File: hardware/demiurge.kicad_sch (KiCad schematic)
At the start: 58 parts, among them J2 PGM, U5 AMS1117-3.3, U6 74LVC1T45W6, U7 CH32V307RCT6, Y1 25MHz

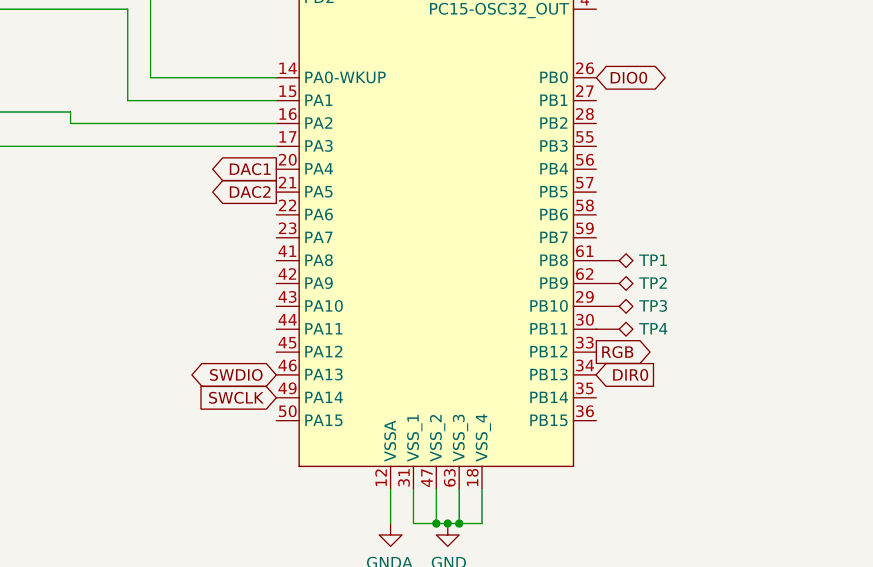
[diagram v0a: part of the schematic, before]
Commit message: Added USB1/USB2 labels. What should we do with 2 USB ports?
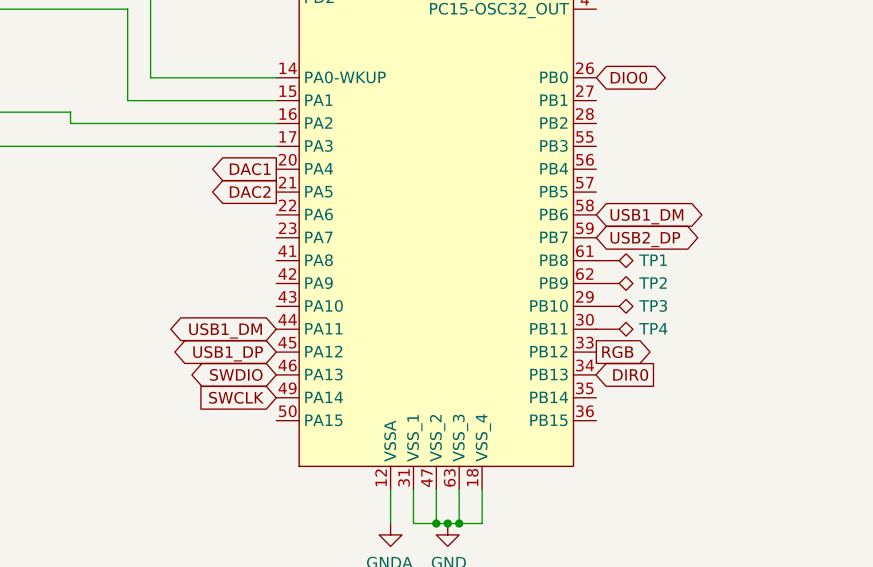
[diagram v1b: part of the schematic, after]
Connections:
- net USB1_DM: now reaches U7.44 (PA11)
- net USB1_DM: now also U7.58 (PB6)
- net USB1_DP: now reaches U7.45 (PA12)
- net USB2_DP: now reaches U7.59 (PB7)
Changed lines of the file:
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@@
+    )
+  )
+  (global_label "USB2_DP" (shape bidirectional) (at 266.7 142.24 0) (fields_autoplaced)
+    (effects (font (size 1.27 1.27)) (justify left))
+    (property "Intersheet References" "${INTERSHEET_REFS}" (id 0) (at 277.5513 142.3194 0)
+      (effects (font (size 1.27 1.27)) (justify left) hide)
     )
   )
@@
     (property "Intersheet References" "${INTERSHEET_REFS}" (id 0) (at 273.6809 93.9006 0)
       (effects (font (size 1.27 1.27)) (justify left) hide)
+    )
+  )
+  (global_label "USB1_DM" (shape bidirectional) (at 231.14 152.4 180) (fields_autoplaced)
+    (effects (font (size 1.27 1.27)) (justify right))
+    (property "Intersheet References" "${INTERSHEET_REFS}" (id 0) (at 220.1072 152.3206 0)
+      (effects (font (size 1.27 1.27)) (justify right) hide)
     )
   )
@@
     (effects (font (size 1.27 1.27)) (justify right))
     (property "Intersheet References" "${INTERSHEET_REFS}" (id 0) (at 342.2691 118.0306 0)
+      (effects (font (size 1.27 1.27)) (justify right) hide)
+    )
+  )
+  (global_label "USB1_DP" (shape bidirectional) (at 231.14 154.94 180) (fields_autoplaced)
+    (effects (font (size 1.27 1.27)) (justify right))
+    (property "Intersheet References" "${INTERSHEET_REFS}" (id 0) (at 220.2887 154.8606 0)
       (effects (font (size 1.27 1.27)) (justify right) hide)
     )
@@
       (effects (font (size 1.27 1.27)) (justify left) hide)
     )
+  )
+  (global_label "USB1_DM" (shape bidirectional) (at 266.7 139.7 0) (fields_autoplaced)
+    (effects (font (size 1.27 1.27)) (justify left))
+    (property "Intersheet References" "${INTERSHEET_REFS}" (id 0) (at 277.7328 139.7794 0)
+      (effects (font (size 1.27 1.27)) (justify left) hide)
+    )

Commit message: First cut of the software. Not changed to RISC-V yet.
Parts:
- removed C16, C19, C2, C8: 100nF, Capacitor_SMD:C_0603_1608Metric, symbol Device:C
- removed R1, R10, R2, R3, R4, R7, R8, R9: 10k, Resistor_SMD:R_0603_1608Metric, symbol Device:R
- removed SW1, SW2, SW3, SW4: ~, Button_Switch_THT:SW_PUSH_6mm_H8mm, symbol Switch:SW_Push
- added D13: ~, Diode_SMD:D_SOD-123, symbol Device:D_Schottky
- added J10: (no value), symbol Connector:USB_C_Receptacle_USB2.0
- added J11: (no value), symbol Connector:USB_A
- added R51: 10k, Resistor_SMD:R_0603_1608Metric, symbol Device:R
- added R52, R53: 5.1k, Resistor_SMD:R_0402_1005Metric, symbol Device:R
- added R54, R55: 22R, Resistor_SMD:R_0402_1005Metric, symbol Device:R
- C31: value 12pF -> 20pF; LCSC C1547 -> C1648
- U6: value 74LVC1T45W6 -> (none); LCSC C168856 -> C441819
- Y1: value 25MHz -> 16MHz; LCSC C90913 -> C13738
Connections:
- net +5V: now also D13.1 (K), J11.1 (VBUS)
- net 0: now also R51.1
- net DIR0: now also U7.27 (PB1)
- net GND: now also J10.A1 (GND), J10.A12 (GND), J10.B1 (GND), J10.B12 (GND), J10.S1 (SHIELD), J11.4 (GND), J11.5 (Shield), R51.2, R52.2, R53.2
- net USB1_DM: now also R54.2; no longer U7.58 (PB6)
- net USB1_DP: now also R55.2
- net USB2_DP: now also J11.3 (D+)
- net at TP3.1: now also U7.53 (PC12); no longer U7.29 (PB10)
- net SWO: now reaches J2.6 (Pin_6)
- net SWO: now also U7.55 (PB3)
- net at TP4.1: now also U7.54 (PD2); no longer U7.30 (PB11)
- net at TP1.1: now also U7.51 (PC10); no longer U7.61 (PB8)
- net at TP2.1: now also U7.52 (PC11); no longer U7.62 (PB9)
- net Pot+LED/GPRST: now reaches U7.34 (PB13)
- net Pot+LED/GPINT: now reaches U7.35 (PB14)
- net LED1: no longer names the net of U7.37 (PC6)
- net LED2: no longer names the net of U7.38 (PC7)
- net LED3: no longer names the net of U7.39 (PC8)
- net LED4: no longer names the net of U7.40 (PC9)
- net RGB: no longer names the net of U7.33 (PB12)
- new net: J10.A5 (CC1), R52.1
- new net: J10.A6 (D+), J10.B6 (D+), R55.1
- new net: J10.A7 (D-), J10.B7 (D-), R54.1
- new net: J10.B5 (CC2), R53.1
- new net Pot+LED/SCL: U7.29 (PB10)
- new net Pot+LED/SDA: U7.30 (PB11)
- new net USB2_DM: J11.2 (D-), U7.58 (PB6)
- new net VBUS: D13.2 (A), J10.A4 (VBUS), J10.A9 (VBUS), J10.B4 (VBUS), J10.B9 (VBUS)
- no-connect marks 8 -> 11
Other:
- sheet Pot+LED ports: added GPINT, GPRST, SCL, SDA; removed LED1, LED2, LED3, LED4, RGB
- note added: "22uF + 100nF at each VDD/VSS pin on CPU"
- note added: "Input Filter"
- note added: "Power"
- note added: "Programming"
- note added: "Unclear if GND and GNDA should be connected externally, or kept separated to avoid ground loop. Keeping this open for now, until we know better."
- note removed: "At input"
- moved on the sheet: C1, C10, C11, C12, C13, C14, C15, C17, C18, C20, C21, C3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

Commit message: Rev E updated to Rev F (WIP)
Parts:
- removed D13: ~, Diode_SMD:D_SOD-123, symbol Device:D_Schottky
- removed J10: (no value), symbol Connector:USB_C_Receptacle_USB2.0
- removed J11: (no value), symbol Connector:USB_A
- removed J2: PGM, Connector_PinHeader_2.54mm:PinHeader_2x03_P2.54mm_Vertical, symbol Connector_Generic:Conn_02x03_Odd_Even
- removed JP2: SolderJumper_2_Open, Jumper:SolderJumper-2_P1.3mm_Open_TrianglePad1.0x1.5mm, symbol Jumper:SolderJumper_2_Open
- removed R51: 10k, Resistor_SMD:R_0603_1608Metric, symbol Device:R
- removed R52: 5.1k, Resistor_SMD:R_0402_1005Metric, symbol Device:R
- removed R55: 22R, Resistor_SMD:R_0402_1005Metric, symbol Device:R
- removed TP1, TP2, TP3, TP4: ~, aaa:TestPoint_THTPad_1.0x1.0mm_Drill0.6mm, symbol Connector:TestPoint_Alt
- removed U7: CH32V307RCT6, Package_QFP:LQFP-64_10x10mm_P0.5mm, symbol awesomeaudio:CH32V307RCT6
- removed Y1: 16MHz, Crystal:Crystal_SMD_3225-4Pin_3.2x2.5mm, symbol Device:Crystal_GND24_Small
- added C17, C18, C2, C20, C22, C23, C24, C27, C35, C36, C8, C9: 100nF, Capacitor_SMD:C_0603_1608Metric, symbol Device:C
- added C28, C29: 20pF, Capacitor_SMD:C_0603_1608Metric, symbol Device:C
- added C38, C39: 1nF, Capacitor_SMD:C_0603_1608Metric, symbol Device:C
- added D1, D5: ~, Diode_SMD:D_SOD-123, symbol Device:D_Schottky
- added D10, D11, D12, D13: ~, LED_THT:LED_D5.0mm-4_RGB, symbol Device:LED_RAGB
- added J11: ~, aaa:USB_C_Receptacle_Vertical, symbol demiurge-rescue:USB_C_Receptacle_USB2.0-Connector
- added J12: Micro_SD_Card_Det_Hirose_DM3AT, Connector_Card:microSD_HC_Hirose_DM3AT-SF-PEJM5, symbol Connector:Micro_SD_Card_Det_Hirose_DM3AT
- added J2: Conn_01x06, Connector_PinHeader_2.54mm:PinHeader_1x06_P2.54mm_Vertical, symbol Connector_Generic:Conn_01x06
- added J3, J4, J5, J6, J8, J9: ~, aaa:PJ301M-12, symbol Connector:AudioJack2_SwitchT
- added JP2, JP3: ~, Jumper:SolderJumper-2_P1.3mm_Open_RoundedPad1.0x1.5mm, symbol Jumper:Jumper_2_Open
- added R1, R10, R13, R2, R29, R3, R37, R38, R4, R47, R48, R7, R8, R9: 10k, Resistor_SMD:R_0603_1608Metric, symbol Device:R
- added R12: 22R, Resistor_SMD:R_0402_1005Metric, symbol Device:R
- added R14, R15: 5.1k, Resistor_SMD:R_0402_1005Metric, symbol Device:R
- added R16, R18: 18k, Resistor_SMD:R_0603_1608Metric, symbol Device:R
- added R17, R19: 13k, Resistor_SMD:R_0603_1608Metric, symbol Device:R
- added R20, R21, R22, R23, R49, R50: 20k, Resistor_SMD:R_0603_1608Metric, symbol Device:R
- added R24, R25, R26, R27: 3k3, Resistor_SMD:R_0603_1608Metric, symbol Device:R
- added R39, R41: 36k, Resistor_SMD:R_0603_1608Metric, symbol Device:R
- added R40, R42: 22k, Resistor_SMD:R_0603_1608Metric, symbol Device:R
- added R44, R46: 33k, Resistor_SMD:R_0603_1608Metric, symbol Device:R
- added RV1, RV2, RV3, RV4: ~, aaa:Potentiometer_Alpha_RD901F-40-00D_Single_Vertical, symbol Device:R_Potentiometer
- added SW1, SW2, SW3, SW4: ~, Button_Switch_THT:SW_PUSH_6mm_H8mm, symbol Switch:SW_Push
- added TP1: TP1, TestPoint:TestPoint_Pad_1.5x1.5mm, symbol Connector:TestPoint
- added TP2: TP2, TestPoint:TestPoint_Pad_1.5x1.5mm, symbol Connector:TestPoint
- added TP3: SWO, TestPoint:TestPoint_Pad_1.5x1.5mm, symbol Connector:TestPoint
- added U1, U3: MCP6002, Package_SO:SOIC-8_3.9x4.9mm_P1.27mm, symbol Amplifier_Operational:TL072
- added U10, U11, U7, U8: TL072, Package_SO:SOIC-8_3.9x4.9mm_P1.27mm, symbol Amplifier_Operational:TL072
- added U13: CH32V307RCT6, Package_QFP:LQFP-64_10x10mm_P0.5mm, symbol awesomeaudio:CH32V307RCT6
- added U4: AW9523BTQR, Package_DFN_QFN:VQFN-24-1EP_4x4mm_P0.5mm_EP2.45x2.45mm, symbol aaa:AW9523BTQR
- added U5: W25Q128JVS, Package_SO:SOIC-8_5.23x5.23mm_P1.27mm, symbol Memory_Flash:W25Q128JVS
- added Y1: 16MHz, Crystal:Crystal_SMD_3225-4Pin_3.2x2.5mm, symbol Device:Crystal
- C1, C3, C4, C5, C6, C7: LCSC C45783 -> C129303
- C10: renamed from C9; LCSC C45783 -> C129303
- C11: renamed from C10; LCSC C45783 -> C129303
- C12: renamed from C11; LCSC C45783 -> C129303
- C13: renamed from C12; LCSC C45783 -> C129303
- C14: renamed from C13; LCSC C45783 -> C129303
- C15: renamed from C14; LCSC C45783 -> C129303
- C16: renamed from C15; LCSC C45783 -> C129303
- C19: renamed from C17; LCSC C45783 -> C129303
- C30: value 12pF -> 100nF; LCSC C1547 -> C14663
- C31: value 20pF -> 100nF; LCSC C1648 -> C14663
- C34: value 22uF -> 100nF; footprint Capacitor_SMD:C_0805_2012Metric -> Capacitor_SMD:C_0603_1608Metric; LCSC C45783 -> C14663
- J1: LCSC (none) -> C68234
- JP1: footprint Jumper:SolderJumper-3_P1.3mm_Bridged12_Pad1.0x1.5mm -> Jumper:SolderJumper-3_P1.3mm_Bridged12_RoundedPad1.0x1.5mm
- R11: value 10k -> 22R; footprint Resistor_SMD:R_0603_1608Metric -> Resistor_SMD:R_0402_1005Metric; LCSC C25804 -> C25092
- R53: value 5.1k -> 100; footprint Resistor_SMD:R_0402_1005Metric -> Resistor_SMD:R_0603_1608Metric; LCSC C25905 -> C22775
- R54: value 22R -> 100; footprint Resistor_SMD:R_0402_1005Metric -> Resistor_SMD:R_0603_1608Metric; LCSC C25092 -> C22775
- U6: value (none) -> 74LVC1T45W6; LCSC C441819 -> C7843
- renumbered C18 to C21, C20 to C25, C21 to C26, D1 to D2, D2 to D3, D3 to D9, R12 to R28, U5 to U2
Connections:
- net +12V: now also C18.1, C20.1, C22.1, C24.1, U10.8 (V+), U11.8 (V+), U7.8 (V+), U8.8 (V+)
- net +3V3: now also C30.1, C31.1, C27.1, C35.1, C36.1, C8.1, D10.2 (A), D11.2 (A), D12.2 (A), D13.2 (A), J12.4 (VDD), JP2.2 (B), R10.2, R13.2, R16.2, R18.2, R2.2, R39.1, R4.2, R41.1, R8.2, RV1.1, RV2.1, RV3.1, RV4.1, U1.8 (V+), U13.1 (VBAT), U13.13 (VDDA), U13.19 (VDD_4), U13.32 (VIO_1), U13.48 (VDD_2), U13.64 (VIO_3), U3.8 (V+), U4.18 (AD0), U4.21 (VCC), U4.24 (AD1), U5.8 (VCC); no longer C32.1, R11.1
- net +5V: now also D1.1 (K), D5.1 (K)
- net -12V: now also C18.2, C20.2, C22.2, C24.2, U10.4 (V-), U11.4 (V-), U7.4 (V-), U8.4 (V-)
- net DIO0: now also U13.23 (PA7)
- net DIR0: now also U13.22 (PA6)
- net GND: now also C17.2, C2.2, C23.2, C27.2, C28.2, C29.2, C35.2, C36.2, C8.2, C9.2, J11.A1 (GND), J11.A12 (GND), J11.B1 (GND), J11.B12 (GND), J11.S1 (SHIELD), J12.11 (SHIELD), J12.6 (VSS), J2.6 (Pin_6), JP3.1 (A), R14.2, R15.2, R29.1, RV1.3, RV2.3, RV3.3, RV4.3, SW1.1, SW2.1, SW3.1, SW4.1, U1.4 (V-), U13.18 (VSS_4), U13.31 (VSS_1), U13.47 (VSS_2), U13.63 (VSS_3), U3.4 (V-), U4.25 (GND), U4.9 (GND), U5.4 (GND); no longer R53.2
- net GNDA: now also J3.S, J3.TN, J4.S, J4.TN, J5.S, J5.TN, J6.S, J6.TN, J8.S, J9.S, R17.1, R19.1, R40.2, R42.2, U10.5 (+), U11.5 (+), U13.12 (VSSA)
- net SWCLK: now also J2.4 (Pin_4), U13.49 (PA14)
- net SWDIO: now also J2.5 (Pin_5), U13.46 (PA13)
- net VBUS: now also D5.2 (A), J11.A4 (VBUS), J11.A9 (VBUS), J11.B4 (VBUS), J11.B9 (VBUS)
- net at R54.1: now also J9.T
- net at R53.1: now also J8.T
- net EN renamed DM
- net DM: now also U13.44 (PA11)
- net USB1_DM: no longer names the net of R54.2
- net USB1_DM: now also C38.2, R49.1, U10.7
- net VIN: no longer names the net of C1.1, C3.1, JP1.2 (C), U2.3 (VI)
- new net: RV1.2, U1.3 (+)
- new net: RV2.2, U1.5 (+)
- new net: RV3.2, U3.3 (+)
- new net: RV4.2, U3.5 (+)
- new net: R1.1, R2.1, SW1.2
- new net: R3.1, R4.1, SW2.2
- new net: R7.1, R8.1, SW3.2
- new net: R10.1, R9.1, SW4.2
- new net: R44.1, R47.2, U10.1
- new net: R37.1, R44.2, U10.2 (-)
- new net: R39.2, R40.1, U10.3 (+)
- new net: C38.1, R47.1, R49.2, U10.6 (-)
- new net: J4.T, R21.2
- new net: J3.T, R20.2
- new net: J5.T, R22.2
- new net: J6.T, R23.2
- new net: R20.1, R24.2, U7.2 (-)
- new net: R16.1, R17.2, U7.3 (+), U7.5 (+)
- new net: R22.1, R26.2, U8.2 (-)
- new net: R18.1, R19.2, U8.3 (+), U8.5 (+)
- new net: R23.1, R27.2, U8.6 (-)
- new net: R21.1, R25.2, U7.6 (-)
- new net: C39.2, R50.1, R53.2, U11.7
- new net: R46.1, R48.2, U11.1
- new net: R38.1, R46.2, U11.2 (-)
- new net: R41.2, R42.1, U11.3 (+)
- new net: C39.1, R48.1, R50.2, U11.6 (-)
- new net: J11.B5 (CC2), R14.1
- new net: J11.A5 (CC1), R15.1
- new net: J11.A6 (D+), J11.B6 (D+), R12.1
- new net: J11.A7 (D-), J11.B7 (D-), R11.1
- new net: C28.1, U13.5 (OSC_IN), Y1.1
- new net: C29.1, U13.6 (OSC_OUT), Y1.2
- new net: D1.2 (A), J2.1 (Pin_1)
- new net AD0: R27.1, U13.24 (PC4), U8.7
- new net AD1: R26.1, U13.25 (PC5), U8.1
- new net AD2: R25.1, U13.26 (PB0), U7.7
- new net AD3: R24.1, U13.27 (PB1), U7.1
- new net AD4: U13.14 (PA0-WKUP), U3.6 (-), U3.7
- new net AD5: U13.15 (PA1), U3.1, U3.2 (-)
- new net AD6: U1.6 (-), U1.7, U13.16 (PA2)
- new net AD7: U1.1, U1.2 (-), U13.17 (PA3)
- new net AO0: R37.2, U13.21 (PA5)
- new net AO1: R38.2, U13.20 (PA4)
- new net B0: C2.1, R1.2, U4.4 (P1_3)
- new net B1: C9.1, R3.2, U4.3 (P1_2)
- new net B2: C17.1, R7.2, U4.2 (P1_1)
- new net B3: C23.1, R9.2, U4.1 (P1_0)
- new net BOOT0: JP2.1 (A), R29.2, U13.60 (BOOT0)
- new net DP: R12.2, U13.45 (PA12)
- new net FLASH_CS: U13.33 (PB12), U5.1 (~{CS})
- new net FLASH_MISO: U13.35 (PB14), U5.2 (DO(IO1))
- new net FLASH_MOSI: U13.36 (PB15), U5.5 (DI(IO0))
- new net FLASH_SCK: U13.34 (PB13), U5.6 (CLK)
- new net GPINT: U13.61 (PB8), U4.22 (INT)
- new net GPRST: U13.62 (PB9), U4.23 (~{RST})
- new net L0_B: D10.4 (BK), U4.5 (P0_0)
- new net L0_G: D10.3 (GK), U4.6 (P0_1)
- new net L0_R: D10.1 (RK), U4.7 (P0_2)
- new net L1_B: D11.4 (BK), U4.8 (P0_3)
- new net L1_G: D11.3 (GK), U4.10 (P0_4)
- new net L1_R: D11.1 (RK), U4.11 (P0_5)
- new net L2_B: D12.4 (BK), U4.12 (P0_6)
- new net L2_G: D12.3 (GK), U4.13 (P0_7)
- new net L2_R: D12.1 (RK), U4.14 (P1_4)
- new net L3_B: D13.4 (BK), U4.15 (P1_5)
- new net L3_G: D13.3 (GK), U4.16 (P1_6)
- new net L3_R: D13.1 (RK), U4.17 (P1_7)
- new net NRST: C32.1, JP3.2 (B), R13.1, U13.7 (NRST)
- new net SCL: U13.58 (PB6), U4.19 (SCL)
- new net SDA: U13.59 (PB7), U4.20 (SDA)
- new net SD_CLK: J12.5 (CLK), U13.53 (PC12)
- new net SD_CMD: J12.3 (CMD), U13.54 (PD2)
- new net SD_D0: J12.7 (DAT0), U13.39 (PC8)
- new net SD_D1: J12.8 (DAT1), U13.40 (PC9)
- new net SD_D2: J12.1 (DAT2), U13.51 (PC10)
- new net SD_D3: J12.2 (DAT3/CD), U13.52 (PC11)
- new net SD_DET: J12.10 (DET_A), J12.9 (DET_B), U13.38 (PC7)
- new net TP1: TP1.1, U13.55 (PB3)
- new net TP2: TP2.1, U13.56 (PB4)
- new net TP3: TP3.1, U13.57 (PB5)
- new net USART1_RX: J2.2 (Pin_2), U13.43 (PA10)
- new net USART1_TX: J2.3 (Pin_3), U13.42 (PA9)
- new net ~{FLASH_HOLD}: U13.9 (PC1), U5.7 (IO3)
- new net ~{FLASH_WP}: U13.8 (PC0), U5.3 (IO2)
- no-connect marks 11 -> 23
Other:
- removed sheet Analog-In1
- removed sheet Analog-In2
- removed sheet Analog-Out1
- removed sheet Analog-Out2
- removed sheet Pot+LED
- note added: "At input"
- note added: "Over opamp supply"
- note removed: "22uF + 100nF at each VDD/VSS pin on CPU"
- note removed: "Input Filter"
- note removed: "Power"
- note removed: "Programming"
- note removed: "Unclear if GND and GNDA should be connected externally, or kept separated to avoid ground loop. Keeping this open for now, until we know better."
- title: Demiurge-V -> Demiurge
- moved on the sheet: C1, C10, C11, C12, C13, C14, C15, C16, C19, C21, C25, C26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
